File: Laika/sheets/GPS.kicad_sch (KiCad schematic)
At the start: 8 parts, among them J8 Conn_01x05, U6 SAM-M8Q

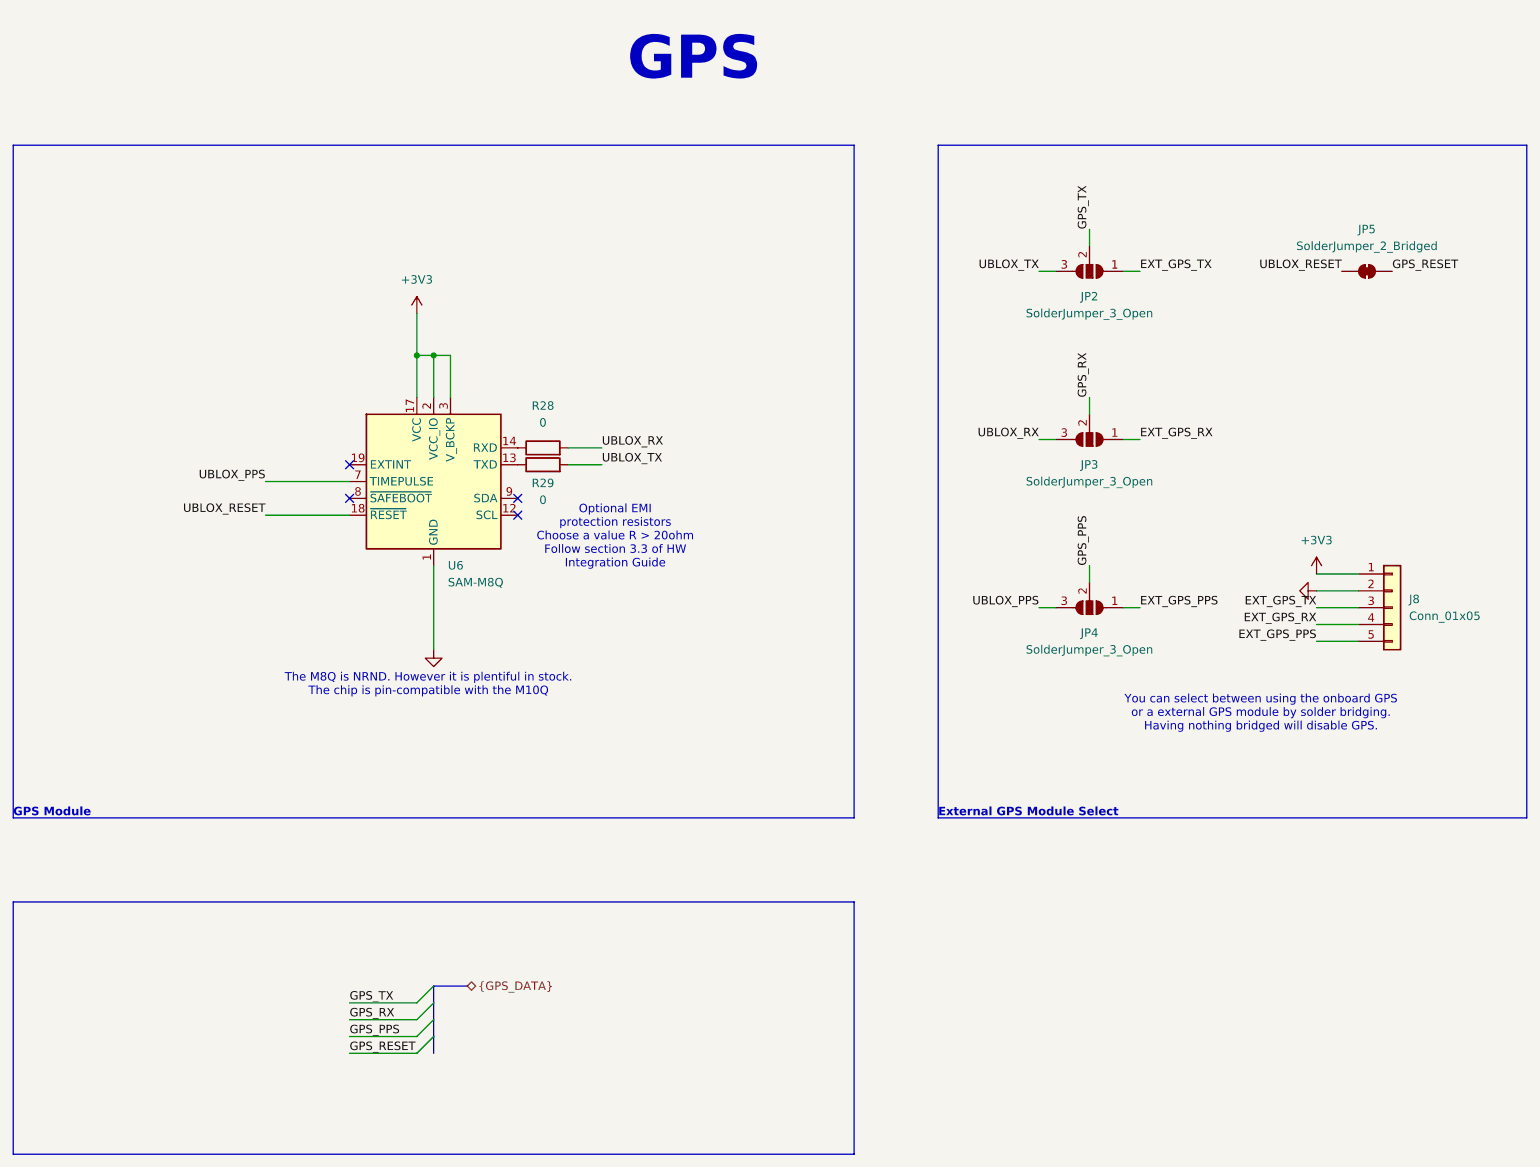
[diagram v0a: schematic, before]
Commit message: Remove external GPS module for spacing constraints
Removed the Ublox GPS module and instead have just a breakout pin
header. While the module technically fit, the amount of free space
around it to follow proper design guidelines left alot of unused space.
To priotize density, GPS design guideslines, and board size, the GPS
will be external.

Signed-off-by: Aeybel Varghese <aeybelvarghese@gmail.com>
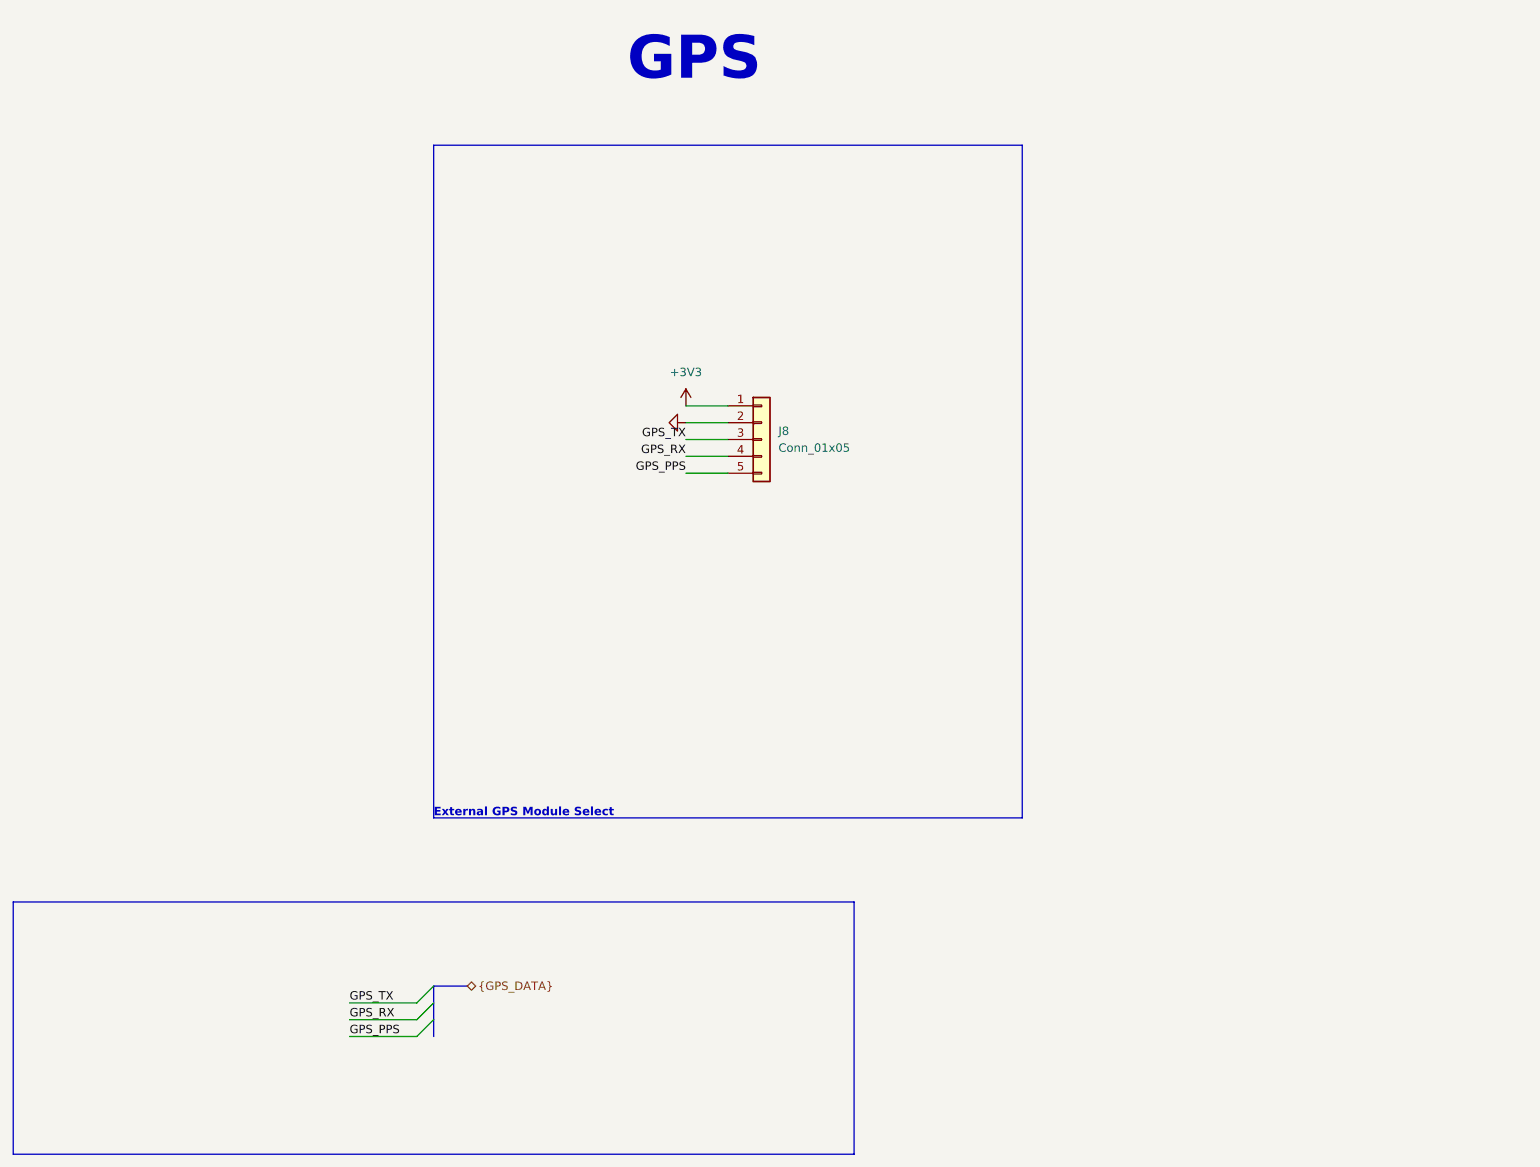
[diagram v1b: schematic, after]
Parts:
- removed JP2, JP3, JP4: SolderJumper_3_Open, Jumper:SolderJumper-3_P1.3mm_Open_Pad1.0x1.5mm, symbol Jumper:SolderJumper_3_Open
- removed JP5: SolderJumper_2_Bridged, Jumper:SolderJumper-2_P1.3mm_Bridged_Pad1.0x1.5mm, symbol Jumper:SolderJumper_2_Bridged
- removed R28, R29: 0, Resistor_SMD:R_0402_1005Metric_Pad0.72x0.64mm_HandSolder, symbol Device:R
- removed U6: SAM-M8Q, RF_GPS:ublox_SAM-M8Q, symbol RF_GPS:SAM-M8Q
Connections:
- net EXT_GPS_PPS is gone; now on net GPS_PPS: J8.5 (Pin_5)
- net EXT_GPS_RX is gone; now on net GPS_RX: J8.4 (Pin_4)
- net EXT_GPS_TX is gone; now on net GPS_TX: J8.3 (Pin_3)
- no-connect marks 4 -> 0
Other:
- note removed: "GPS Module"
- note removed: "Optional EMI protection resistors Choose a value R > 20ohm Follow section 3.3 of HW Integration Guide"
- note removed: "The M8Q is NRND. However it is plentiful in stock. The chip is pin-compatible with the M10Q"
- note removed: "You can select between using the onboard GPS or a external GPS module by solder bridging. Having nothing bridged will disable GPS."
- moved on the sheet: J8
